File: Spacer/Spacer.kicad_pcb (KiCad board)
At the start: 2 copper layers, 21 x 4 mm, 0 parts

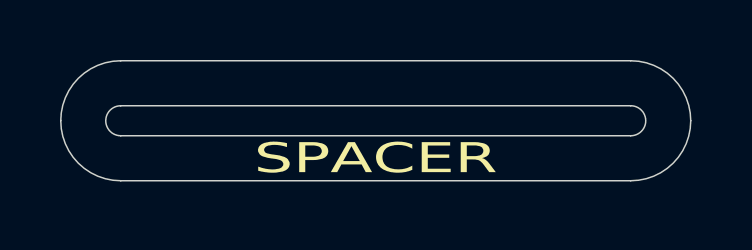
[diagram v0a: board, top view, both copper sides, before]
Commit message: Update files to KiCAD 7.
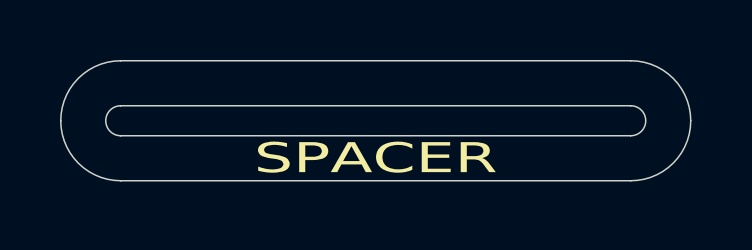
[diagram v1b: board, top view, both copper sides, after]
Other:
- net class Default removed
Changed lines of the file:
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@@
-(kicad_pcb (version 20171130) (host pcbnew 5.1.5-1.fc31)
+(kicad_pcb (version 20221018) (generator pcbnew)
   (general
     (thickness 1.6)
-    (drawings 18)
-    (tracks 0)
-    (zones 0)
-    (modules 0)
-    (nets 1)
   )
-  (page USLetter)
+  (paper "USLetter")
   (title_block
     (title "NucleoTNC Spacer")
-    (date 2020-05-05)
-    (rev B)
+    (date "2020-05-05")
+    (rev "B")
     (company "Mobilinkd TNC")
     (comment 1 "1.6mm FR4")
   )
   (layers
-    (0 F.Cu signal)
-    (31 B.Cu signal)
-    (32 B.Adhes user)
-    (33 F.Adhes user)
-    (34 B.Paste user)
-    (35 F.Paste user)
-    (36 B.SilkS user)
-    (37 F.SilkS user)
-    (38 B.Mask user)
-    (39 F.Mask user)
-    (40 Dwgs.User user)
-    (41 Cmts.User user)
-    (42 Eco1.User user)
-    (43 Eco2.User user)
-    (44 Edge.Cuts user)
-    (45 Margin user)
-    (46 B.CrtYd user)
-    (47 F.CrtYd user)
-    (48 B.Fab user)
-    (49 F.Fab user)
+    (0 "F.Cu" signal)
+    (31 "B.Cu" signal)
+    (32 "B.Adhes" user "B.Adhesive")
+    (33 "F.Adhes" user "F.Adhesive")
+    (34 "B.Paste" user)
+    (35 "F.Paste" user)
+    (36 "B.SilkS" user "B.Silkscreen")
+    (37 "F.SilkS" user "F.Silkscreen")
+    (38 "B.Mask" user)
+    (39 "F.Mask" user)
+    (40 "Dwgs.User" user "User.Drawings")
+    (41 "Cmts.User" user "User.Comments")
+    (42 "Eco1.User" user "User.Eco1")
+    (43 "Eco2.User" user "User.Eco2")
+    (44 "Edge.Cuts" user)
+    (45 "Margin" user)
+    (46 "B.CrtYd" user "B.Courtyard")
+    (47 "F.CrtYd" user "F.Courtyard")
+    (48 "B.Fab" user)
+    (49 "F.Fab" user)
   )
   (setup
-    (last_trace_width 0.25)
-    (trace_clearance 0.2)
-    (zone_clearance 0.508)
-    (zone_45_only no)
-    (trace_min 0.2)
-    (via_size 0.8)
-    (via_drill 0.4)
-    (via_min_size 0.4)
-    (via_min_drill 0.3)
-    (uvia_size 0.3)
-    (uvia_drill 0.1)
-    (uvias_allowed no)
-    (uvia_min_size 0.2)
-    (uvia_min_drill 0.1)
-    (edge_width 0.05)
-    (segment_width 0.2)
-    (pcb_text_width 0.3)
-    (pcb_text_size 1.5 1.5)
-    (mod_edge_width 0.12)
-    (mod_text_size 1 1)
-    (mod_text_width 0.15)
-    (pad_size 1.524 1.524)
-    (pad_drill 0.762)
     (pad_to_mask_clearance 0.051)
     (solder_mask_min_width 0.25)
-    (aux_axis_origin 0 0)
-    (visible_elements FFFFFF7F)
     (pcbplotparams
-      (layerselection 0x210e0_7ffffffe)
+      (layerselection 0x00210e0_7ffffffe)
+      (plot_on_all_layers_selection 0x0000000_00000000)
+      (disableapertmacros false)
       (usegerberextensions false)
       (usegerberattributes false)
       (usegerberadvancedattributes false)
       (creategerberjobfile false)
-      (excludeedgelayer true)
-      (linewidth 0.100000)
+      (dashed_line_dash_ratio 12.000000)
+      (dashed_line_gap_ratio 3.000000)
+      (svgprecision 4)
       (plotframeref false)
       (viasonmask false)
@@
       (hpglpenspeed 20)
       (hpglpendiameter 15.000000)
+      (dxfpolygonmode true)
+      (dxfimperialunits true)
+      (dxfusepcbnewfont true)
       (psnegative false)
       (psa4output false)
@@
       (plotvalue true)
       (plotinvisibletext false)
-      (padsonsilk false)
+      (sketchpadsonfab false)
       (subtractmaskfromsilk false)
       (outputformat 1)
@@
       (drillshape 0)
       (scaleselection 1)
-      (outputdirectory "Gerbers/"))
+      (outputdirectory "Gerbers/")
+    )
   )
   (net 0 "")
-  (net_class Default "This is the default net class."
-    (clearance 0.2)
-    (trace_width 0.25)
-    (via_dia 0.8)
-    (via_drill 0.4)
-    (uvia_dia 0.3)
-    (uvia_drill 0.1)
+  (gr_arc (start 152 88) (mid 150.585786 87.414214) (end 150 86)
+    (stroke (width 0.05) (type solid)) (layer "Edge.Cuts"))
+  (gr_line (start 152 84) (end 169 84)
+    (stroke (width 0.05) (type solid)) (layer "Edge.Cuts"))
+  (gr_arc (start 171 86) (mid 170.414214 87.414214) (end 169 88)
+    (stroke (width 0.05) (type solid)) (layer "Edge.Cuts"))
+  (gr_arc (start 169 84) (mid 170.414214 84.585786) (end 171 86)
+    (stroke (width 0.05) (type solid)) (layer "Edge.Cuts"))
+  (gr_arc (start 150 86) (mid 150.585786 84.585786) (end 152 84)
+    (stroke (width 0.05) (type solid)) (layer "Edge.Cuts"))
+  (gr_line (start 152 88) (end 169 88)
+    (stroke (width 0.05) (type solid)) (layer "Edge.Cuts"))
+  (gr_line (start 152 86.5) (end 169 86.5)
+    (stroke (width 0.05) (type solid)) (layer "Edge.Cuts"))
+  (gr_arc (start 152 86.5) (mid 151.5 86) (end 152 85.5)
+    (stroke (width 0.05) (type solid)) (layer "Edge.Cuts"))
+  (gr_arc (start 169 85.5) (mid 169.5 86) (end 169 86.5)
+    (stroke (width 0.05) (type solid)) (layer "Edge.Cuts"))
+  (gr_line (start 152 85.5) (end 169 85.5)
+    (stroke (width 0.05) (type solid)) (layer "Edge.Cuts"))
+  (gr_circle (center 161 84.75) (end 161 85.25)
+    (stroke (width 0.15) (type solid)) (fill none) (layer "F.Fab"))
+  (gr_line (start 161.5 84.5) (end 164 82.5)
+    (stroke (width 0.15) (type solid)) (layer "F.Fab"))
+  (gr_line (start 164 82.5) (end 165.25 82.5)
+    (stroke (width 0.15) (type solid)) (layer "F.Fab"))
+  (gr_text "SPACER" (at 160.5 87.25) (layer "F.SilkS")
+    (effects (font (size 1 1.5) (thickness 0.1)))
   )
-  (dimension 21.001488 (width 0.15) (layer Dwgs.User)
-    (gr_text "21.001 mm" (at 160.625508 96.417645 0.6820603932) (layer Dwgs.User)
+  (gr_text "Please place Production Code here on front silkscreen." (at 164 81.75) (layer "F.Fab")
+    (effects (font (size 1 1) (thickness 0.15)))
+  )
+  (dimension (type aligned) (layer "Dwgs.User")
+    (pts (xy 165.75 88) (xy 165.75 84))
+    (height 9.75)
+    (gr_text "4.0000 mm" (at 174.35 86 90) (layer "Dwgs.User")
       (effects (font (size 1 1) (thickness 0.15)))
     )
-    (feature1 (pts (xy 171 85.75) (xy 171.117013 95.579116)))
-    (feature2 (pts (xy 150 86) (xy 150.117013 95.829116)))
-    (crossbar (pts (xy 150.110033 95.242737) (xy 171.110033 94.992737)))
-    (arrow1a (pts (xy 171.110033 94.992737) (xy 169.99059 95.592526)))
-    (arrow1b (pts (xy 171.110033 94.992737) (xy 169.976628 94.419768)))
-    (arrow2a (pts (xy 150.110033 95.242737) (xy 151.243438 95.815706)))
-    (arrow2b (pts (xy 150.110033 95.242737) (xy 151.229476 94.642948)))
+    (format (prefix "") (suffix "") (units 2) (units_format 1) (precision 4))
+    (style (thickness 0.12) (arrow_length 1.27) (text_position_mode 0) (extension_height 0.58642) (extension_offset 0) keep_text_aligned)
   )
-  (gr_text "Please place Production Code here on front silkscreen." (at 164 81.75) (layer F.Fab)
-    (effects (font (size 1 1) (thickness 0.15)))
-  )
-  (gr_line (start 164 82.5) (end 165.25 82.5) (layer F.Fab) (width 0.15))
-  (gr_line (start 161.5 84.5) (end 164 82.5) (layer F.Fab) (width 0.15))
-  (gr_circle (center 161 84.75) (end 161 85.25) (layer F.Fab) (width 0.15))
-  (dimension 18 (width 0.15) (layer Dwgs.User)
-    (gr_text "18.000 mm" (at 160.5 92.05) (layer Dwgs.User)
+  (dimension (type aligned) (layer "Dwgs.User")
+    (pts (xy 171 85.75) (xy 150 86))
+    (height -9.243391)
+    (gr_text "21.0015 mm" (at 160.596343 93.967817 0.6820603932) (layer "Dwgs.User")
       (effects (font (size 1 1) (thickness 0.15)))
     )
-    (feature1 (pts (xy 151.5 86) (xy 151.5 91.336421)))
-    (feature2 (pts (xy 169.5 86) (xy 169.5 91.336421)))
-    (crossbar (pts (xy 169.5 90.75) (xy 151.5 90.75)))
-    (arrow1a (pts (xy 151.5 90.75) (xy 152.626504 90.163579)))
-    (arrow1b (pts (xy 151.5 90.75) (xy 152.626504 91.336421)))
-    (arrow2a (pts (xy 169.5 90.75) (xy 168.373496 90.163579)))
-    (arrow2b (pts (xy 169.5 90.75) (xy 168.373496 91.336421)))
+    (format (prefix "") (suffix "") (units 2) (units_format 1) (precision 4))
+    (style (thickness 0.15) (arrow_length 1.27) (text_position_mode 0) (extension_height 0.58642) (extension_offset 0) keep_text_aligned)
   )
-  (gr_arc (start 169 86) (end 169 86.5) (angle -180) (layer Edge.Cuts) (width 0.05))
-  (gr_arc (start 152 86) (end 152 85.5) (angle -180) (layer Edge.Cuts) (width 0.05))
-  (gr_line (start 152 86.5) (end 169 86.5) (layer Edge.Cuts) (width 0.05))
-  (gr_line (start 152 85.5) (end 169 85.5) (layer Edge.Cuts) (width 0.05))
-  (dimension 4 (width 0.12) (layer Dwgs.User)
-    (gr_text "4.000 mm" (at 176.77 86 270) (layer Dwgs.User)
+  (dimension (type aligned) (layer "Dwgs.User")
+    (pts (xy 151.5 86) (xy 169.5 86))
+    (height 4.75)
+    (gr_text "18.0000 mm" (at 160.5 89.6) (layer "Dwgs.User")
       (effects (font (size 1 1) (thickness 0.15)))
     )
-    (feature1 (pts (xy 165.75 88) (xy 176.086421 88)))
-    (feature2 (pts (xy 165.75 84) (xy 176.086421 84)))
-    (crossbar (pts (xy 175.5 84) (xy 175.5 88)))
-    (arrow1a (pts (xy 175.5 88) (xy 174.913579 86.873496)))
-    (arrow1b (pts (xy 175.5 88) (xy 176.086421 86.873496)))
-    (arrow2a (pts (xy 175.5 84) (xy 174.913579 85.126504)))
-    (arrow2b (pts (xy 175.5 84) (xy 176.086421 85.126504)))
+    (format (prefix "") (suffix "") (units 2) (units_format 1) (precision 4))
+    (style (thickness 0.15) (arrow_length 1.27) (text_position_mode 0) (extension_height 0.58642) (extension_offset 0) keep_text_aligned)
   )
-  (gr_text SPACER (at 160.5 87.25) (layer F.SilkS)
-    (effects (font (size 1 1.5) (thickness 0.1)))
-  )
-  (gr_arc (start 169 86) (end 169 88) (angle -90) (layer Edge.Cuts) (width 0.05))
-  (gr_arc (start 152 86) (end 150 86) (angle -90) (layer Edge.Cuts) (width 0.05))
-  (gr_arc (start 169 86) (end 171 86) (angle -90) (layer Edge.Cuts) (width 0.05))
-  (gr_arc (start 152 86) (end 152 84) (angle -90) (layer Edge.Cuts) (width 0.05))
-  (gr_line (start 152 88) (end 169 88) (layer Edge.Cuts) (width 0.05))
-  (gr_line (start 152 84) (end 169 84) (layer Edge.Cuts) (width 0.05))
 )
